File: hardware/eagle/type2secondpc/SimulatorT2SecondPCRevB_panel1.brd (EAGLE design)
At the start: 48.3 x 48.3 mm, 13 parts

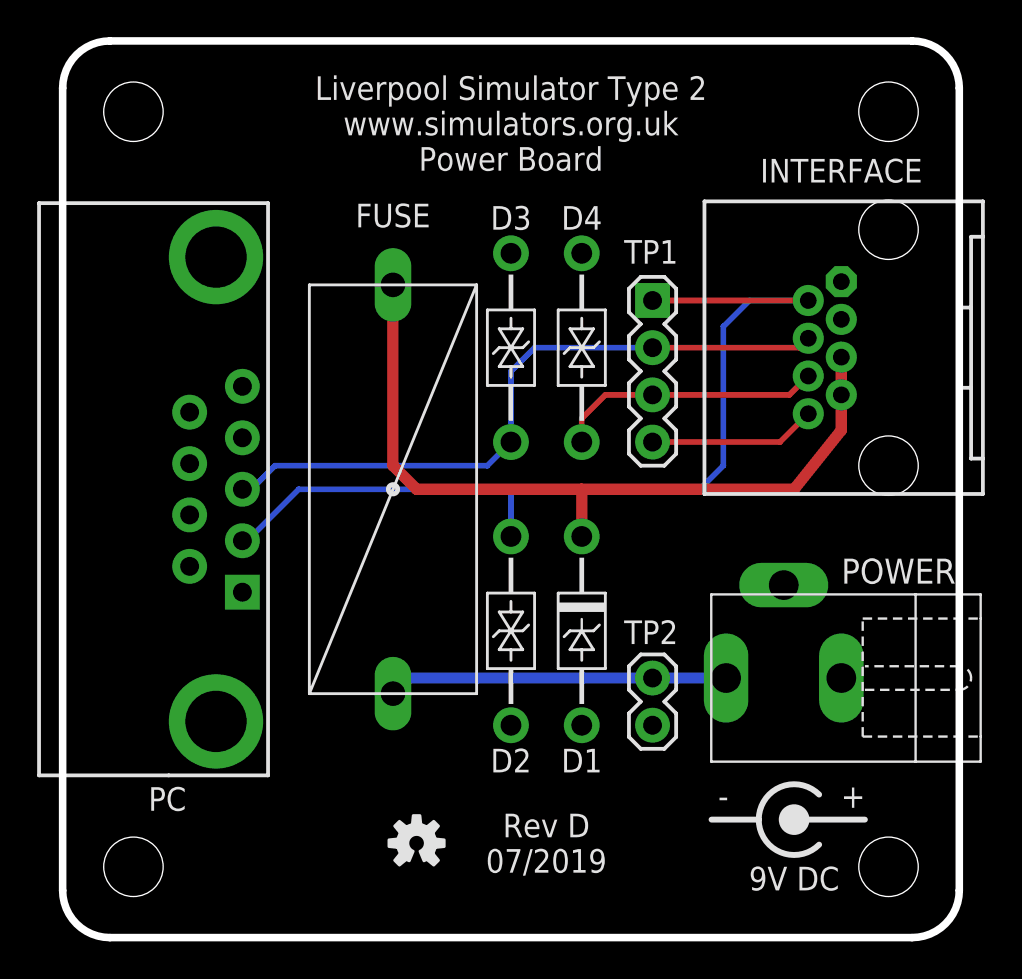
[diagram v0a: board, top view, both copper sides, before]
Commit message: Board Housekeeping
URL on silkscreens, caution messages, tidy up naming conventions.
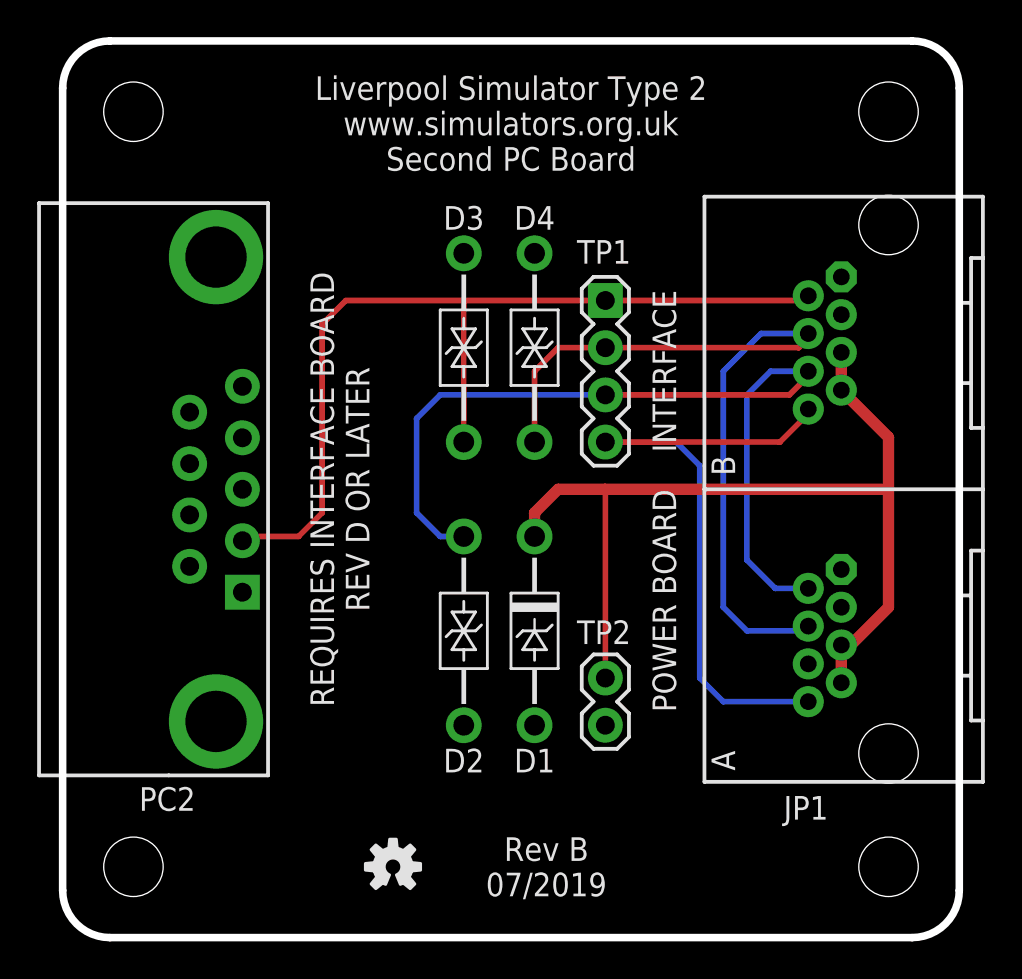
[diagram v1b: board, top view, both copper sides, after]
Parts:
- removed FUSE: 800mA, AIC_Custom:MCOMP-FUSE-HOLDER-PCB
- removed INTERFACE: RJ45-RJHSE-X08090DEG, AIC_Custom:RJ45-RJHSE-5080
- removed POWER: 9V DC, AIC_Custom:CLIFF-FC681465P-DC-JACK
- removed U$1: (no value), AIC_Custom:CENTRE-POS-SILK
- added JP1: RJ45-RJHSE-5080-022HOLE, AIC_Custom:RJ45-RJHSE-5080-02
- moved D1 2.54 mm to (25.4, 16.5)
- moved D4 2.54 mm to (25.4, 31.8)
- moved D2 2.54 mm to (21.6, 16.5)
- moved D3 2.54 mm to (21.6, 31.8)
- moved TP1 2.54 mm to (29.2, 34.3)
- moved TP2 2.54 mm to (29.2, 14.0)
- moved LOGO1 1.80 mm to (17.8, 3.81)
- renumbered PC to PC2, U$2 to E$1
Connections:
- removed net VIN: FUSE.2, POWER.1, TP2.1
- net GND: now also JP1.A1, JP1.A3, JP1.B1, JP1.B3; no longer INTERFACE.1, INTERFACE.3, POWER.3
- net P8: now also JP1.A8, JP1.B8; no longer INTERFACE.8
- net RXD: now also D4.C, JP1.A4, JP1.B4; no longer D3.C, INTERFACE.4, PC2.3
- net TX2: now also D2.C, JP1.A2, JP1.B6; no longer D4.C, INTERFACE.6
- net TXD: now also D3.C, JP1.B2; no longer D2.C, INTERFACE.2
- net VIN2: now also JP1.A5, JP1.A7, JP1.B5, JP1.B7, TP2.1; no longer FUSE.1, INTERFACE.5, INTERFACE.7
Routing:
- net TX2: track 14.4 -> 47.1 mm
- net P8: track 9.01 -> 35.2 mm
- net VIN: track 18.3 -> 0.00 mm
- net VIN2: track 42.4 -> 51.2 mm
- net RXD: track 36.1 -> 42.8 mm
- net TXD: track 51.1 -> 49.5 mm
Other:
- board text added: "D1"
- board text added: "D2"
- board text added: "D3"
- board text added: "D4"
- board text added: "JP1"
- board text added: "Liverpool Simulator Type 2 www.simulators.org.uk Second PC Board"
- board text added: "PC2"
- board text added: "POWER BOARD INTERFACE"
- board text added: "REQUIRES INTERFACE BOARD REV D OR LATER"
- board text added: "Rev B 07/2019"
- board text added: "TP1"
- board text added: "TP2"
- board text removed: "Liverpool Simulator Type 2 www.simulators.org.uk Power Board"
- board text removed: "Rev D 07/2019"
